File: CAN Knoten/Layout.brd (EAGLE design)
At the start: 112.9 x 61.3 mm, 41 parts, among them IC1 74LS165D, IC2 74LS165D, K1 68711614522, K2 68711614522, K3 68711614522, K4 68711614522, Q1 HC49-U - 16MHz, Q2 HC49-U - xMHz

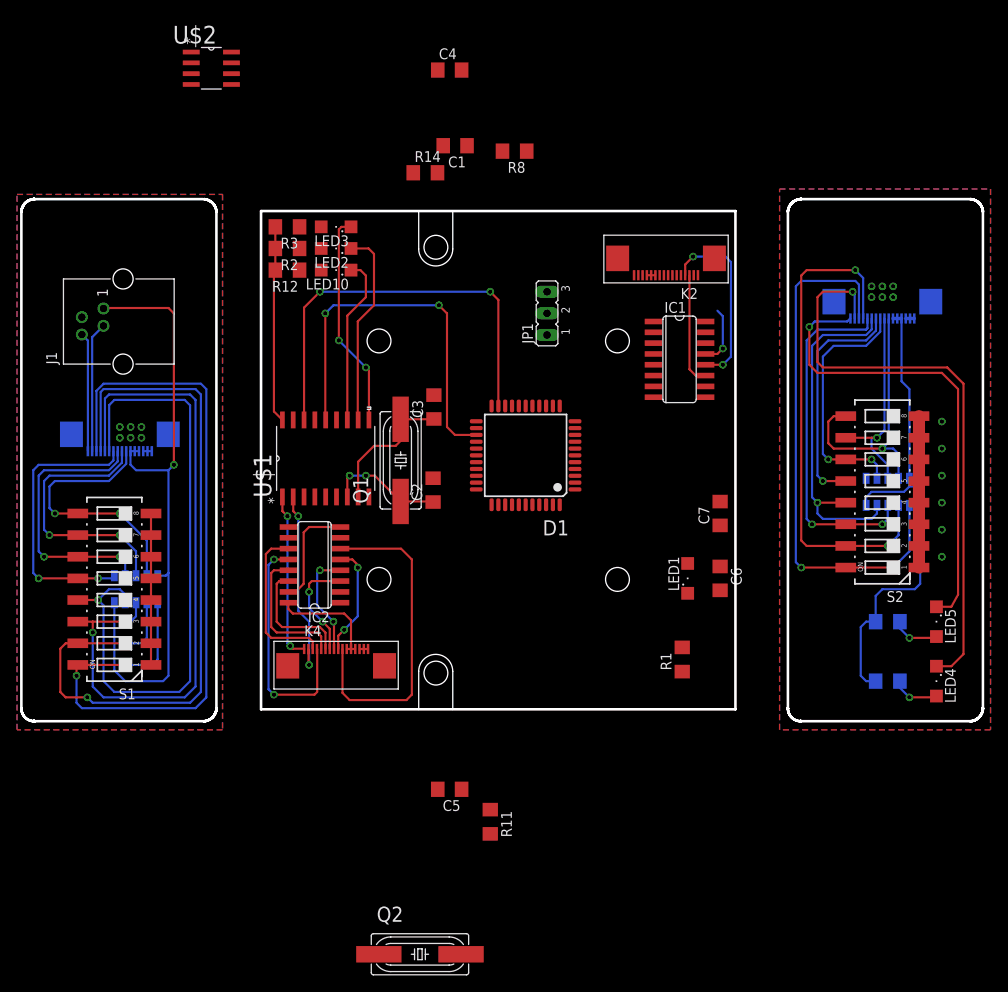
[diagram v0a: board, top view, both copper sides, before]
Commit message: 
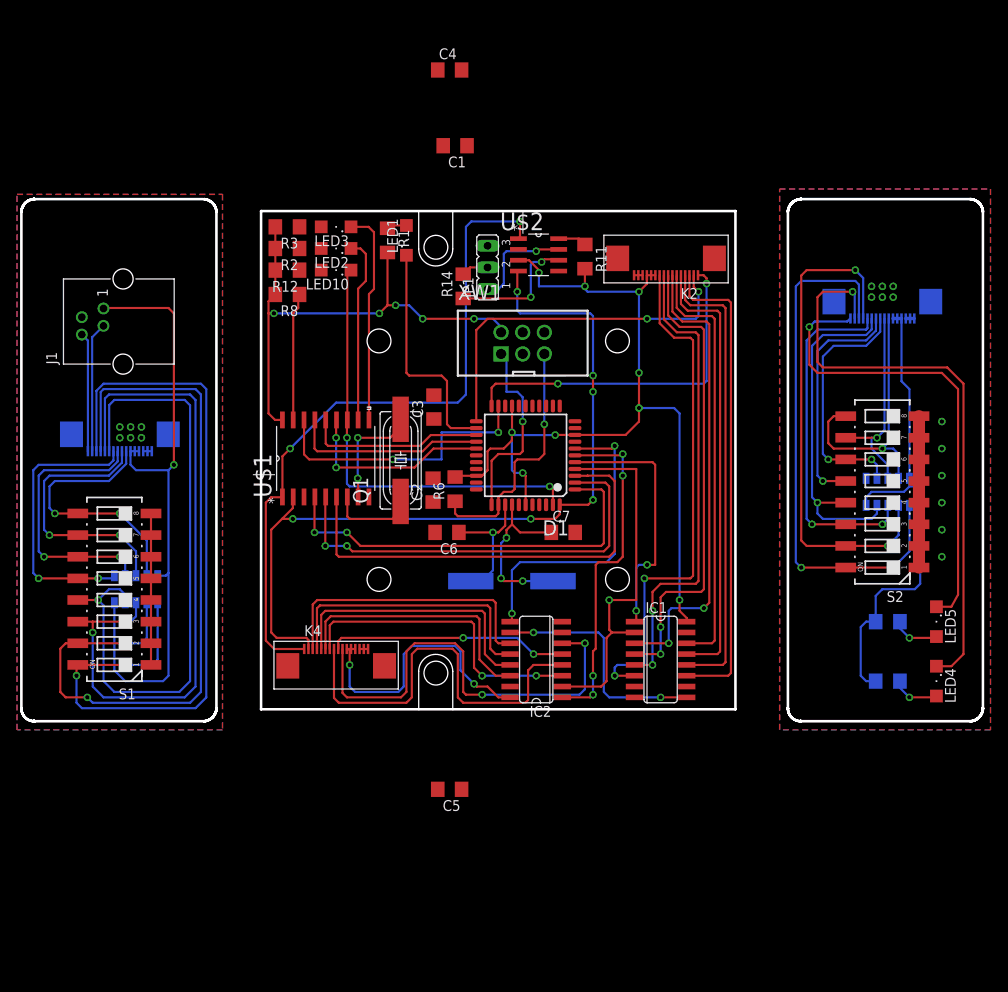
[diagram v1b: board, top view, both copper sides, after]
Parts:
- added R6: 10k, rcl:R1206
- added XW1: (no value), Atmel - ISP_6 (AVR ISP MKII):WSL
- moved R11 67.3 mm to (84.8, 13.0)
- moved R1 60.2 mm to (61.6, 14.9), turned to 270 degrees
- moved LED1 51.6 mm to (63.8, 14.9)
- moved Q2 45.1 mm to (76.2, -25.1), flipped to the bottom
- moved U$2 44.2 mm to (79.3, 13.2)
- moved IC1 35.3 mm to (93.7, -34.3)
- moved C6 32.5 mm to (68.6, -19.4), turned to 180 degrees
- moved R8 31.5 mm to (49.8, 8.57)
- moved IC2 28.3 mm to (79.1, -34.3)
- moved C7 18.5 mm to (82.2, -19.4), turned to 0 degrees
- moved R14 14.1 mm to (70.5, 9.53), turned to 90 degrees
- moved JP1 8.83 mm to (73.3, 11.7)
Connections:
- new net N$31: D1.35, R6.1, XW1.5
- new net XMEGA_PDI_DATA: D1.34, XW1.1
- net GND: now also XW1.6
- net VCC: now also R6.2, XW1.2
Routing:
- net VCC: track 37.2 -> 199.5 mm, vias 0 -> 16
- net MCP2515_RXCAN: track 22.4 -> 96.3 mm, vias 2 -> 6
- net MCP2515_TXCAN: track 19.7 -> 81.0 mm
- net NODE_ID_7: track 0.00 -> 60.9 mm, vias 0 -> 2
- net NODE_ID_6: track 0.00 -> 55.5 mm, vias 0 -> 2
- net NODE_ID_5: track 0.00 -> 55.3 mm, vias 0 -> 2
- net NODE_ID_4: track 0.00 -> 54.9 mm, vias 0 -> 2
- net MCP2515_TX2RTS: track 0.00 -> 53.0 mm
- net MCP2515_TX1RTS: track 0.00 -> 50.8 mm, vias 0 -> 2
- net NODE_ID_3: track 0.00 -> 50.0 mm
- net MCP2515_TX0RTS: track 0.00 -> 48.5 mm, vias 0 -> 2
- net NODE_ID_2: track 6.98 -> 52.2 mm, vias 1 -> 0
- net 74XX165_CLK: track 0.00 -> 43.8 mm, vias 0 -> 1
- net NODE_ID_0: track 13.3 -> 56.5 mm
- net DEBUG_TXD: track 0.00 -> 42.5 mm, vias 0 -> 2
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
